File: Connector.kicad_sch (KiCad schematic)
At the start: 3 parts, among them J6 Conn_01x10, J7 Conn_01x10, J8 Conn_01x02

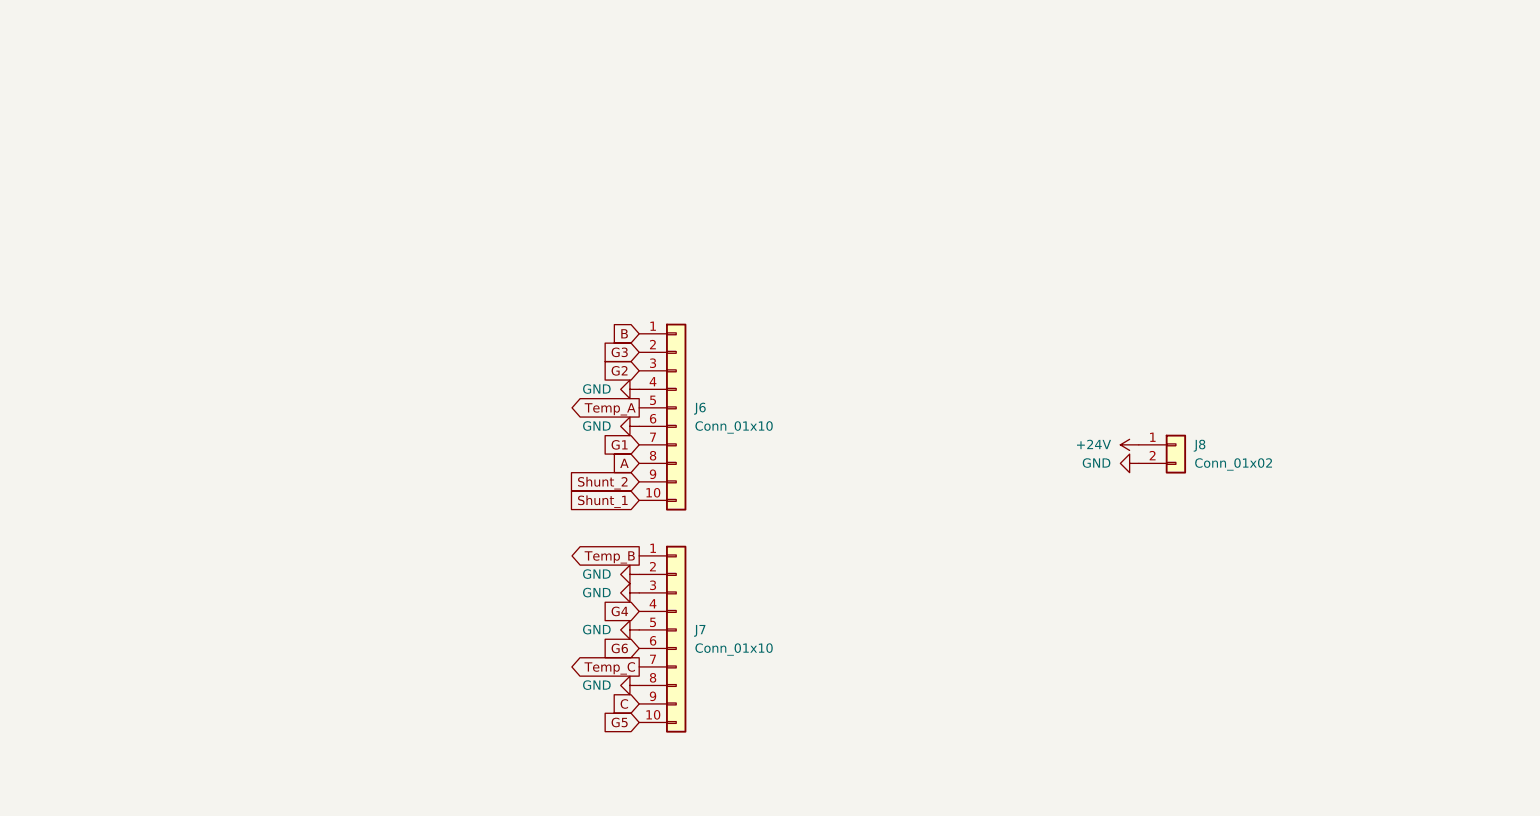
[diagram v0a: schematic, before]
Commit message: Добавил крепежные отверстия
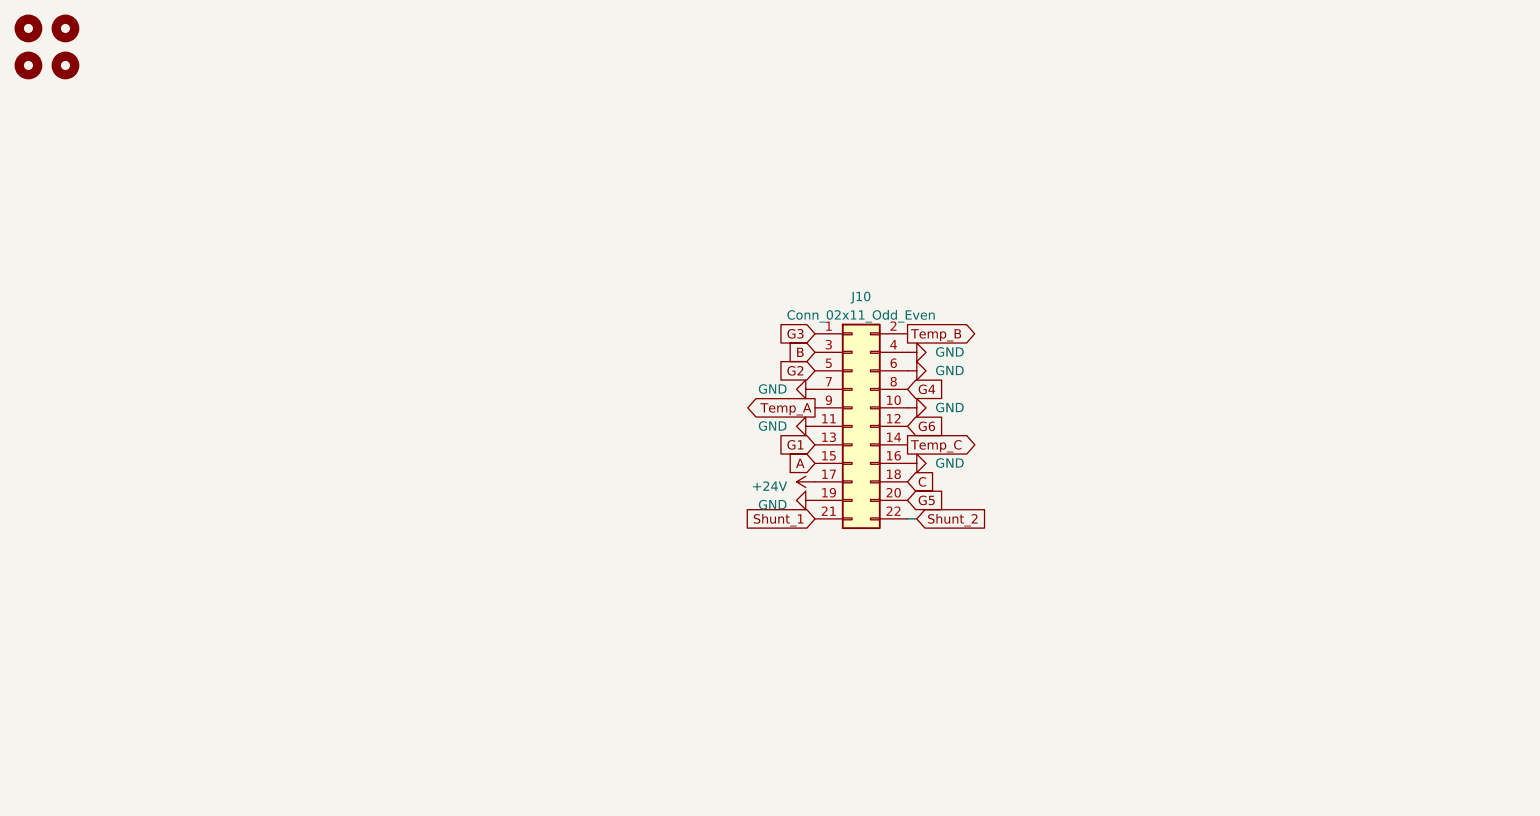
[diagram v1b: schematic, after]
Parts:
- removed J6, J7: Conn_01x10, Connector_PinHeader_2.54mm:PinHeader_1x10_P2.54mm_Vertical, symbol Connector_Generic:Conn_01x10
- removed J8: Conn_01x02, Connector_PinHeader_2.54mm:PinHeader_1x02_P2.54mm_Vertical_SMD_Pin1Left, symbol Connector_Generic:Conn_01x02
- added H1, H2, H3, H4: MountingHole, MountingHole:MountingHole_3.2mm_M3, symbol Mechanical:MountingHole
- added J10: Conn_02x11_Odd_Even, Connector_PinSocket_2.54mm:PinSocket_2x11_P2.54mm_Vertical, symbol Connector_Generic:Conn_02x11_Odd_Even
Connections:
- net +24V: now also J10.17 (Pin_17)
- net A: now also J10.15 (Pin_15)
- net B: now also J10.3 (Pin_3)
- net C: now also J10.18 (Pin_18)
- net G1: now also J10.13 (Pin_13)
- net G2: now also J10.5 (Pin_5)
- net G3: now also J10.1 (Pin_1)
- net G4: now also J10.8 (Pin_8)
- net G5: now also J10.20 (Pin_20)
- net G6: now also J10.12 (Pin_12)
- net GND: now also J10.10 (Pin_10), J10.11 (Pin_11), J10.16 (Pin_16), J10.19 (Pin_19), J10.4 (Pin_4), J10.6 (Pin_6), J10.7 (Pin_7)
- net Shunt_1: now also J10.21 (Pin_21)
- net Shunt_2: now also J10.22 (Pin_22)
- net Temp_A: now also J10.9 (Pin_9)
- net Temp_B: now also J10.2 (Pin_2)
- net Temp_C: now also J10.14 (Pin_14)

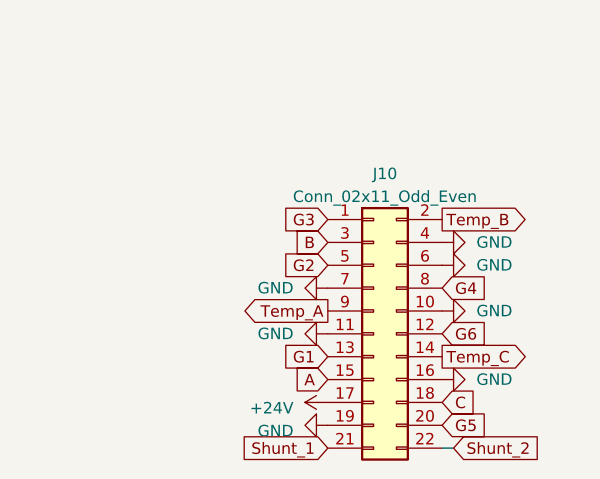
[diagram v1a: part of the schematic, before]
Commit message: Поменял NTC на цифровые датчики
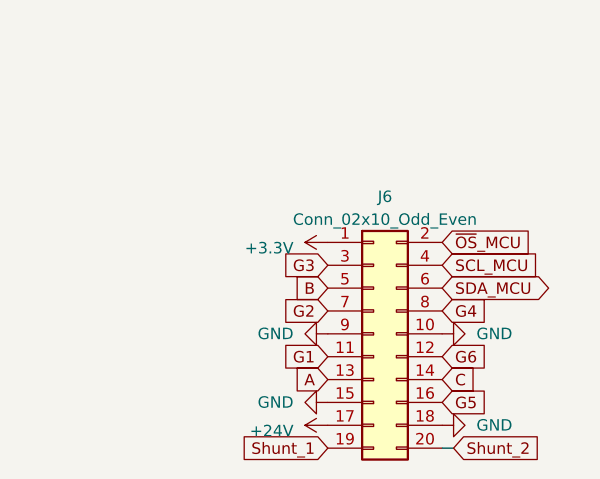
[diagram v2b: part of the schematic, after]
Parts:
- removed J10: Conn_02x11_Odd_Even, Connector_PinSocket_2.54mm:PinSocket_2x11_P2.54mm_Vertical, symbol Connector_Generic:Conn_02x11_Odd_Even
- added J6: Conn_02x10_Odd_Even, Connector_PinSocket_2.54mm:PinSocket_2x10_P2.54mm_Vertical, symbol Connector_Generic:Conn_02x10_Odd_Even
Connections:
- net +24V: now also J6.17 (Pin_17)
- net A: now also J6.13 (Pin_13)
- net B: now also J6.5 (Pin_5)
- net C: now also J6.14 (Pin_14)
- net G1: now also J6.11 (Pin_11)
- net G2: now also J6.7 (Pin_7)
- net G3: now also J6.3 (Pin_3)
- net G4: now also J6.8 (Pin_8)
- net G5: now also J6.16 (Pin_16)
- net G6: now also J6.12 (Pin_12)
- net GND: now also J6.10 (Pin_10), J6.15 (Pin_15), J6.18 (Pin_18), J6.9 (Pin_9)
- net Shunt_1: now also J6.19 (Pin_19)
- net Shunt_2: now also J6.20 (Pin_20)
- new net +3.3V: J6.1 (Pin_1)
- new net SCL_MCU: J6.4 (Pin_4)
- new net SDA_MCU: J6.6 (Pin_6)
- new net ~{OS}_MCU: J6.2 (Pin_2)

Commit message: Отчётная версия
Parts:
- removed H3, H4: MountingHole, MountingHole:MountingHole_3.2mm_M3, symbol Mechanical:MountingHole
- renumbered J6 to J7
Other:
- note added: "Соединительный разъём"
- company: (none) -> Московский Политех
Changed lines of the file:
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@@
 (kicad_sch (version 20230121) (generator eeschema)
   (paper "A4")
+  (title_block
+    (company "Московский Политех")
+    (comment 1 "МПСТ.76721.758764.01.Э3.М")
+  )
   (wire (pts (xy 163.83 96.52) (xy 165.1 96.52))
     (stroke (width 0) (type default))
   )
+  (rectangle (start 132.08 63.5) (end 182.88 107.95)
+    (stroke (width 0) (type dash))
+    (fill (type none))
+  )
+  (text "Соединительный разъём" (at 132.08 62.23 0)
+    (effects (font (size 3.5 3.5)) (justify left bottom))
+  )
   (global_label "C" (shape input) (at 163.83 88.9 0) (fields_autoplaced)
     (effects (font (size 1.27 1.27)) (justify left))
@@
   (symbol (lib_id "power:GND") (at 151.13 91.44 270) (unit 1)
     (in_bom yes) (on_board yes) (dnp no) (fields_autoplaced)
-    (property "Reference" "#PWR018" (at 144.78 91.44 0)
+    (property "Reference" "#PWR019" (at 144.78 91.44 0)
       (effects (font (size 1.27 1.27)) hide)
     )
@@
       (project "Силовая плата"
         (path "/96c6fc92-8ec6-44f7-b0dc-9ad8f1acea09/a27b443f-c036-4fd6-934c-6ea912709de0"
-          (reference "#PWR018") (unit 1)
+          (reference "#PWR019") (unit 1)
+        )
+        (path "/96c6fc92-8ec6-44f7-b0dc-9ad8f1acea09/e8223907-1cc2-45fb-8266-c61760002ef3"
+          (reference "#PWR038") (unit 1)
         )
       )
@@
   )
   (symbol (lib_id "Connector_Generic:Conn_02x10_Odd_Even") (at 156.21 83.82 0) (unit 1)
-    (in_bom yes) (on_board yes) (dnp no) (fields_autoplaced)
-    (property "Reference" "J6" (at 157.48 68.58 0)
+    (in_bom yes) (on_board yes) (dnp no)
+    (property "Reference" "J7" (at 157.48 71.12 0)
       (effects (font (size 1.27 1.27)))
     )
     (property "Value" "Conn_02x10_Odd_Even" (at 157.48 71.12 0)
-      (effects (font (size 1.27 1.27)))
+      (effects (font (size 1.27 1.27)) hide)
     )
     (property "Footprint" "Connector_PinSocket_2.54mm:PinSocket_2x10_P2.54mm_Vertical" (at 156.21 83.82 0)
@@
       (project "Силовая плата"
         (path "/96c6fc92-8ec6-44f7-b0dc-9ad8f1acea09/a27b443f-c036-4fd6-934c-6ea912709de0"
-          (reference "J6") (unit 1)
-        )
-      )
-    )
-  )
-  (symbol (lib_id "Mechanical:MountingHole") (at 48.26 34.29 0) (unit 1)
-    (in_bom yes) (on_board yes) (dnp no) (fields_autoplaced)
-    (property "Reference" "H4" (at 50.8 33.655 0)
-      (effects (font (size 1.27 1.27)) (justify left) hide)
-    )
-    (property "Value" "MountingHole" (at 50.8 36.195 0)
-      (effects (font (size 1.27 1.27)) (justify left) hide)
-    )
-    (property "Footprint" "MountingHole:MountingHole_3.2mm_M3" (at 48.26 34.29 0)
-      (effects (font (size 1.27 1.27)) hide)
-    )
-    (property "Datasheet" "~" (at 48.26 34.29 0)
-      (effects (font (size 1.27 1.27)) hide)
-    )
-    (instances
-      (project "Силовая плата"
-        (path "/96c6fc92-8ec6-44f7-b0dc-9ad8f1acea09/a27b443f-c036-4fd6-934c-6ea912709de0"
-          (reference "H4") (unit 1)
-        )
-      )
-    )
-  )
-  (symbol (lib_id "Mechanical:MountingHole") (at 43.18 34.29 0) (unit 1)
-    (in_bom yes) (on_board yes) (dnp no) (fields_autoplaced)
-    (property "Reference" "H3" (at 45.72 33.655 0)
-      (effects (font (size 1.27 1.27)) (justify left) hide)
-    )
-    (property "Value" "MountingHole" (at 45.72 36.195 0)
-      (effects (font (size 1.27 1.27)) (justify left) hide)
-    )
-    (property "Footprint" "MountingHole:MountingHole_3.2mm_M3" (at 43.18 34.29 0)
-      (effects (font (size 1.27 1.27)) hide)
-    )
-    (property "Datasheet" "~" (at 43.18 34.29 0)
-      (effects (font (size 1.27 1.27)) hide)
-    )
-    (instances
-      (project "Силовая плата"
-        (path "/96c6fc92-8ec6-44f7-b0dc-9ad8f1acea09/a27b443f-c036-4fd6-934c-6ea912709de0"
-          (reference "H3") (unit 1)
+          (reference "J7") (unit 1)
+        )
+        (path "/96c6fc92-8ec6-44f7-b0dc-9ad8f1acea09/e8223907-1cc2-45fb-8266-c61760002ef3"
+          (reference "J9") (unit 1)
         )
       )
@@
         )
         (path "/96c6fc92-8ec6-44f7-b0dc-9ad8f1acea09/a27b443f-c036-4fd6-934c-6ea912709de0"
-          (reference "#PWR023") (unit 1)
+          (reference "#PWR020") (unit 1)
+        )
+        (path "/96c6fc92-8ec6-44f7-b0dc-9ad8f1acea09/e8223907-1cc2-45fb-8266-c61760002ef3"
+          (reference "#PWR039") (unit 1)
         )
       )
@@
   (symbol (lib_id "power:+3.3V") (at 151.13 73.66 90) (unit 1)
     (in_bom yes) (on_board yes) (dnp no) (fields_autoplaced)
-    (property "Reference" "#PWR042" (at 154.94 73.66 0)
+    (property "Reference" "#PWR016" (at 154.94 73.66 0)
       (effects (font (size 1.27 1.27)) hide)
     )
@@
       (project "Силовая плата"
         (path "/96c6fc92-8ec6-44f7-b0dc-9ad8f1acea09/a27b443f-c036-4fd6-934c-6ea912709de0"
-          (reference "#PWR042") (unit 1)
-        )
-      )
-    )
-  )
-  (symbol (lib_id "Mechanical:MountingHole") (at 48.26 29.21 0) (unit 1)
-    (in_bom yes) (on_board yes) (dnp no) (fields_autoplaced)
-    (property "Reference" "H2" (at 50.8 28.575 0)
-      (effects (font (size 1.27 1.27)) (justify left) hide)
-    )
-    (property "Value" "MountingHole" (at 50.8 31.115 0)
-      (effects (font (size 1.27 1.27)) (justify left) hide)
-    )
-    (property "Footprint" "MountingHole:MountingHole_3.2mm_M3" (at 48.26 29.21 0)
-      (effects (font (size 1.27 1.27)) hide)
-    )
-    (property "Datasheet" "~" (at 48.26 29.21 0)
+          (reference "#PWR016") (unit 1)
+        )
+        (path "/96c6fc92-8ec6-44f7-b0dc-9ad8f1acea09/e8223907-1cc2-45fb-8266-c61760002ef3"
+          (reference "#PWR035") (unit 1)
+        )
+      )
+    )
+  )
+  (symbol (lib_id "Mechanical:MountingHole") (at 158.75 133.35 0) (unit 1)
+    (in_bom yes) (on_board yes) (dnp no) (fields_autoplaced)
+    (property "Reference" "H2" (at 161.29 132.715 0)
+      (effects (font (size 1.27 1.27)) (justify left) hide)
+    )
+    (property "Value" "MountingHole" (at 161.29 135.255 0)
+      (effects (font (size 1.27 1.27)) (justify left) hide)
+    )
+    (property "Footprint" "MountingHole:MountingHole_3.2mm_M3" (at 158.75 133.35 0)
+      (effects (font (size 1.27 1.27)) hide)
+    )
+    (property "Datasheet" "~" (at 158.75 133.35 0)
       (effects (font (size 1.27 1.27)) hide)
     )
@@
         (path "/96c6fc92-8ec6-44f7-b0dc-9ad8f1acea09/a27b443f-c036-4fd6-934c-6ea912709de0"
           (reference "H2") (unit 1)
+        )
+        (path "/96c6fc92-8ec6-44f7-b0dc-9ad8f1acea09/e8223907-1cc2-45fb-8266-c61760002ef3"
+          (reference "H4") (unit 1)
         )
       )
@@
           (reference "#PWR017") (unit 1)
         )
-      )
-    )
-  )
-  (symbol (lib_id "Mechanical:MountingHole") (at 43.18 29.21 0) (unit 1)
-    (in_bom yes) (on_board yes) (dnp no) (fields_autoplaced)
-    (property "Reference" "H1" (at 45.72 28.575 0)
-      (effects (font (size 1.27 1.27)) (justify left) hide)
-    )
-    (property "Value" "MountingHole" (at 45.72 31.115 0)
-      (effects (font (size 1.27 1.27)) (justify left) hide)
-    )
-    (property "Footprint" "MountingHole:MountingHole_3.2mm_M3" (at 43.18 29.21 0)
-      (effects (font (size 1.27 1.27)) hide)
-    )
-    (property "Datasheet" "~" (at 43.18 29.21 0)
+        (path "/96c6fc92-8ec6-44f7-b0dc-9ad8f1acea09/e8223907-1cc2-45fb-8266-c61760002ef3"
+          (reference "#PWR036") (unit 1)
+        )
+      )
+    )
+  )
+  (symbol (lib_id "Mechanical:MountingHole") (at 153.67 133.35 0) (unit 1)
+    (in_bom yes) (on_board yes) (dnp no) (fields_autoplaced)
+    (property "Reference" "H1" (at 156.21 132.715 0)
+      (effects (font (size 1.27 1.27)) (justify left) hide)
+    )
+    (property "Value" "MountingHole" (at 156.21 135.255 0)
+      (effects (font (size 1.27 1.27)) (justify left) hide)
+    )
+    (property "Footprint" "MountingHole:MountingHole_3.2mm_M3" (at 153.67 133.35 0)
+      (effects (font (size 1.27 1.27)) hide)
+    )
+    (property "Datasheet" "~" (at 153.67 133.35 0)
       (effects (font (size 1.27 1.27)) hide)
     )
@@
           (reference "H1") (unit 1)
         )
+        (path "/96c6fc92-8ec6-44f7-b0dc-9ad8f1acea09/e8223907-1cc2-45fb-8266-c61760002ef3"
+          (reference "H3") (unit 1)
+        )
       )
     )
@@
   (symbol (lib_id "power:GND") (at 163.83 83.82 90) (mirror x) (unit 1)
     (in_bom yes) (on_board yes) (dnp no) (fields_autoplaced)
-    (property "Reference" "#PWR019" (at 170.18 83.82 0)
+    (property "Reference" "#PWR018" (at 170.18 83.82 0)
       (effects (font (size 1.27 1.27)) hide)
     )
@@
       (project "Силовая плата"
         (path "/96c6fc92-8ec6-44f7-b0dc-9ad8f1acea09/a27b443f-c036-4fd6-934c-6ea912709de0"
-          (reference "#PWR019") (unit 1)
+          (reference "#PWR018") (unit 1)
+        )
+        (path "/96c6fc92-8ec6-44f7-b0dc-9ad8f1acea09/e8223907-1cc2-45fb-8266-c61760002ef3"
+          (reference "#PWR037") (unit 1)
         )
       )
@@
   (symbol (lib_id "power:GND") (at 163.83 93.98 90) (mirror x) (unit 1)
     (in_bom yes) (on_board yes) (dnp no) (fields_autoplaced)
-    (property "Reference" "#PWR022" (at 170.18 93.98 0)
+    (property "Reference" "#PWR021" (at 170.18 93.98 0)
       (effects (font (size 1.27 1.27)) hide)
     )
@@
       (project "Силовая плата"
         (path "/96c6fc92-8ec6-44f7-b0dc-9ad8f1acea09/a27b443f-c036-4fd6-934c-6ea912709de0"
-          (reference "#PWR022") (unit 1)
-        )
-      )
+          (reference "#PWR021") (unit 1)
+        )
+        (path "/96c6fc92-8ec6-44f7-b0dc-9ad8f1acea09/e8223907-1cc2-45fb-8266-c61760002ef3"
+          (reference "#PWR040") (unit 1)
+        )
+      )
